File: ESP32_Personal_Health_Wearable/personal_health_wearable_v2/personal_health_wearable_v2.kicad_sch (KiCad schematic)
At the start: 26 parts, among them J1 TYPE-C-31-M-12, J2 Conn_01x04_RA, SW1 SMD_4.6x2.8mm_h1.9mm, SW2 SMD_4.6x2.8mm_h1.9mm, U1 ESP32-C6-MINI-1, U2 USBLC6-2SC6, U3 TPS63001

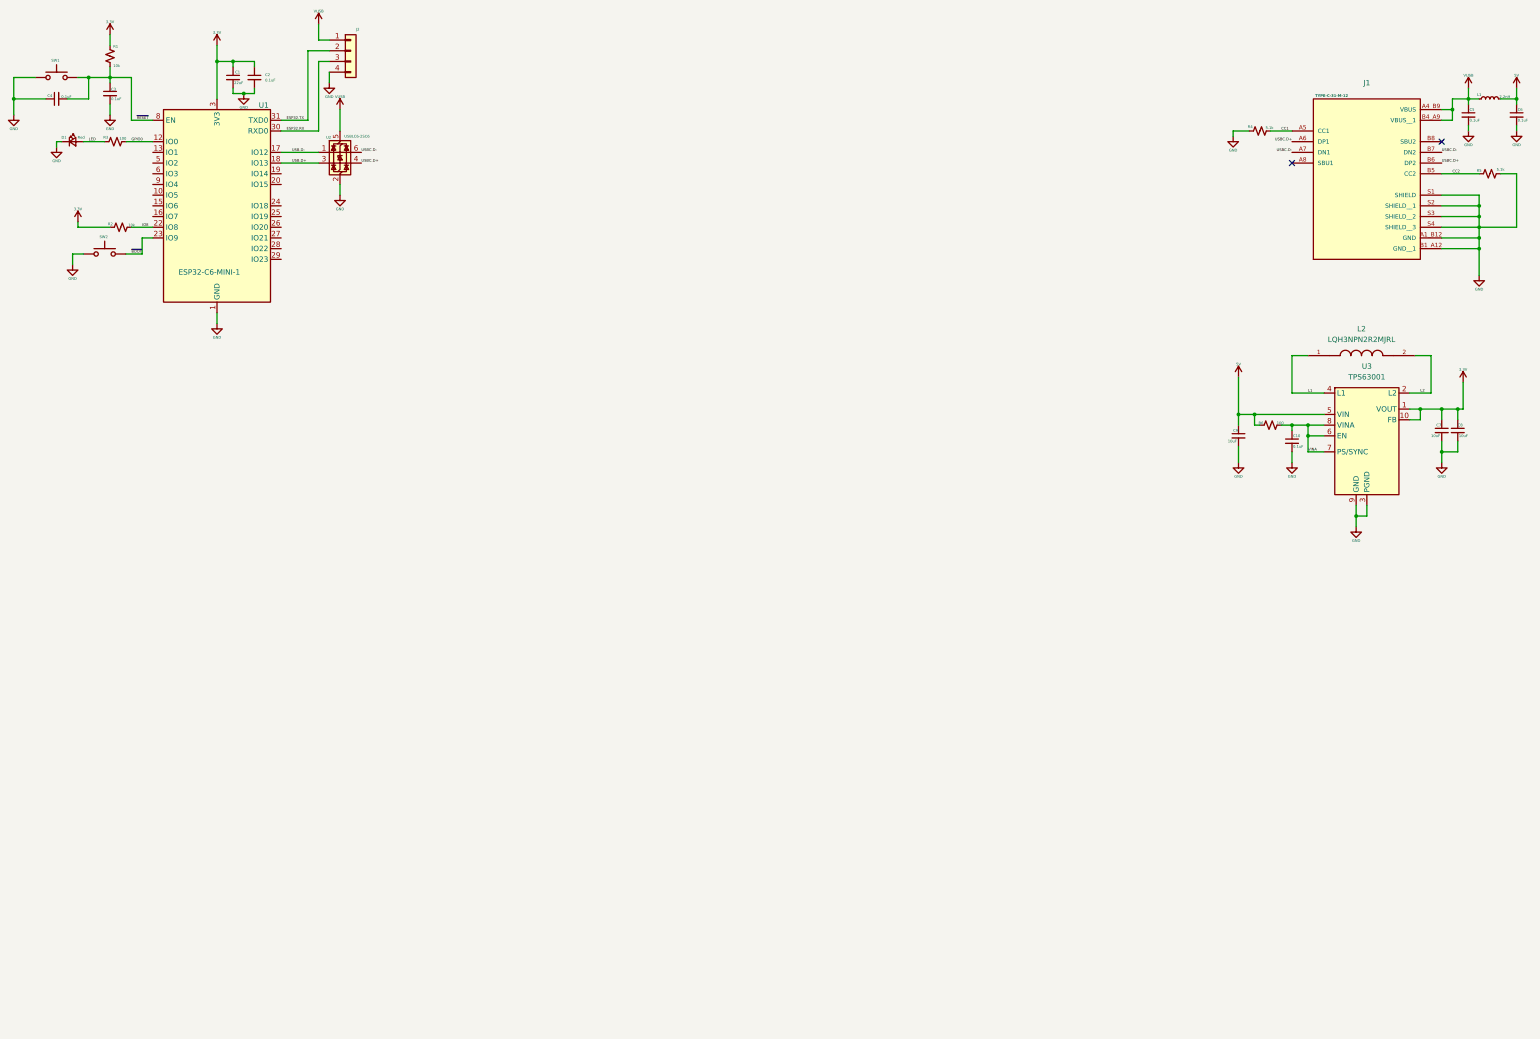
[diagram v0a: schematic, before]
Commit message: Routed i2c connections
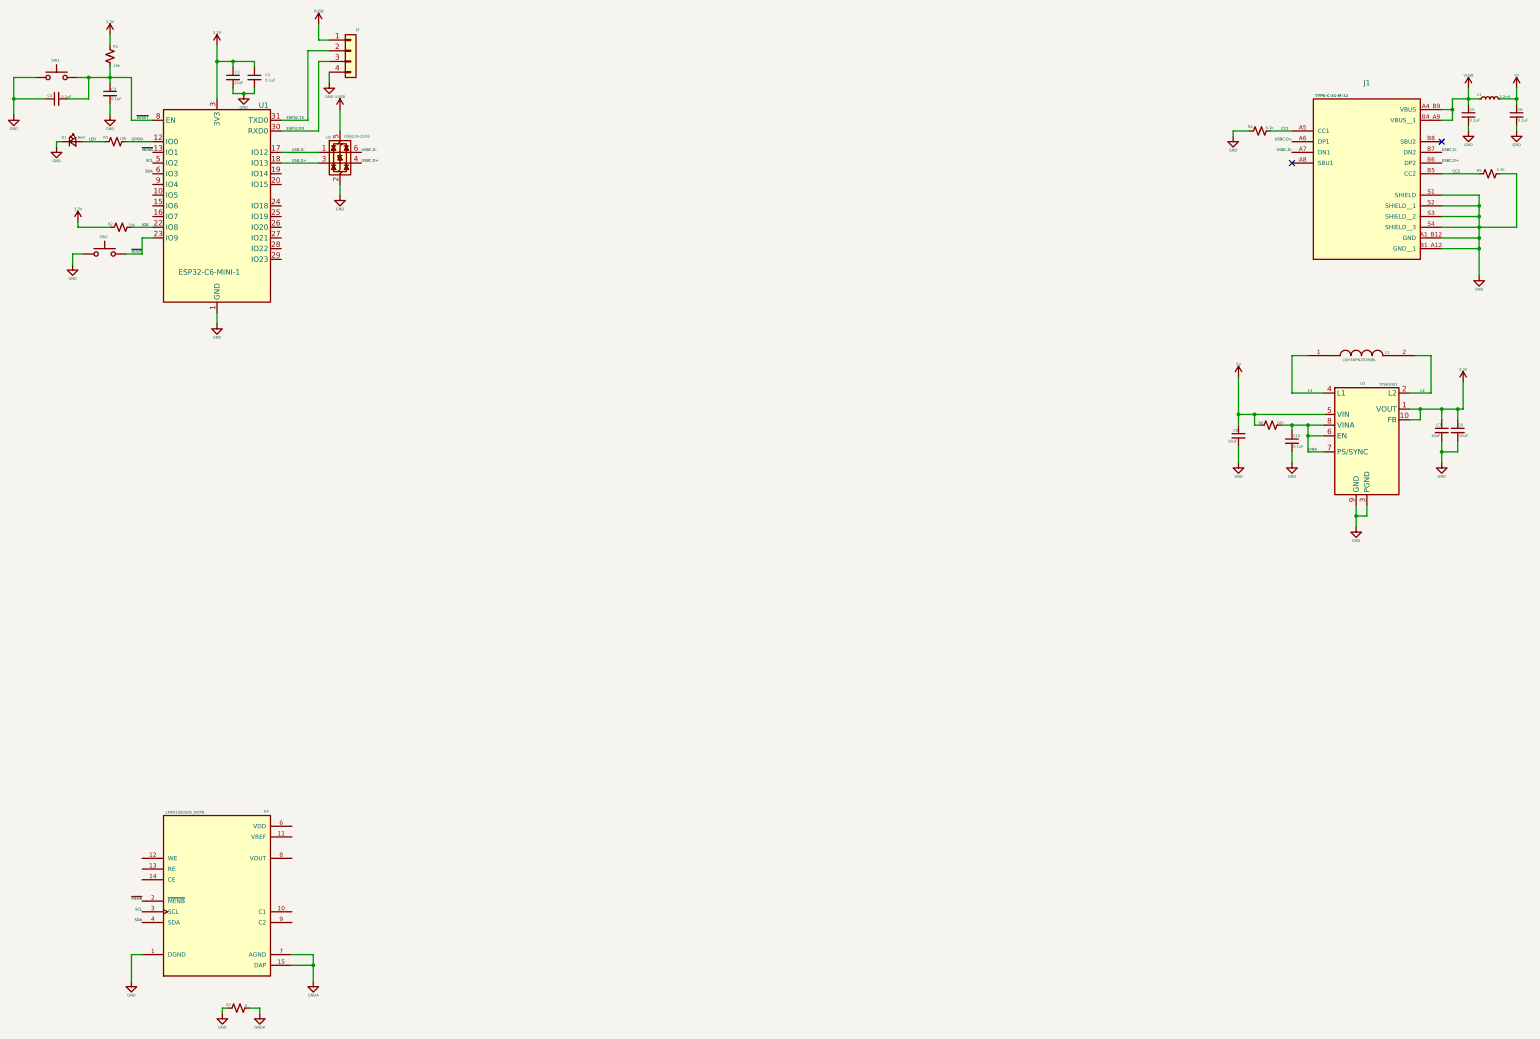
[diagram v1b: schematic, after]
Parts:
- added R7: 0, Resistor_SMD:R_0402_1005Metric, symbol SparkFun-Resistor:0_0402
- added U4: LMP91000SDE_NOPB, LMP91000SDE_NOPB:SON50P400X400X80-15N, symbol LMP91000SDE_NOPB:LMP91000SDE_NOPB
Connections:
- net GND: now also R7.1, U4.1 (DGND)
- net ~{MENB}: now reaches U1.13 (IO1)
- net ~{MENB}: now also U4.2 (~{MENB})
- net SCL: now reaches U1.5 (IO2)
- net SCL: now also U4.3 (SCL)
- net SDA: now reaches U1.6 (IO3)
- net SDA: now also U4.4 (SDA)
- new net GNDA: R7.2, U4.15 (DAP), U4.7 (AGND)
